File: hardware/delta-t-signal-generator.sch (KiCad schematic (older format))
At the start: 28 parts

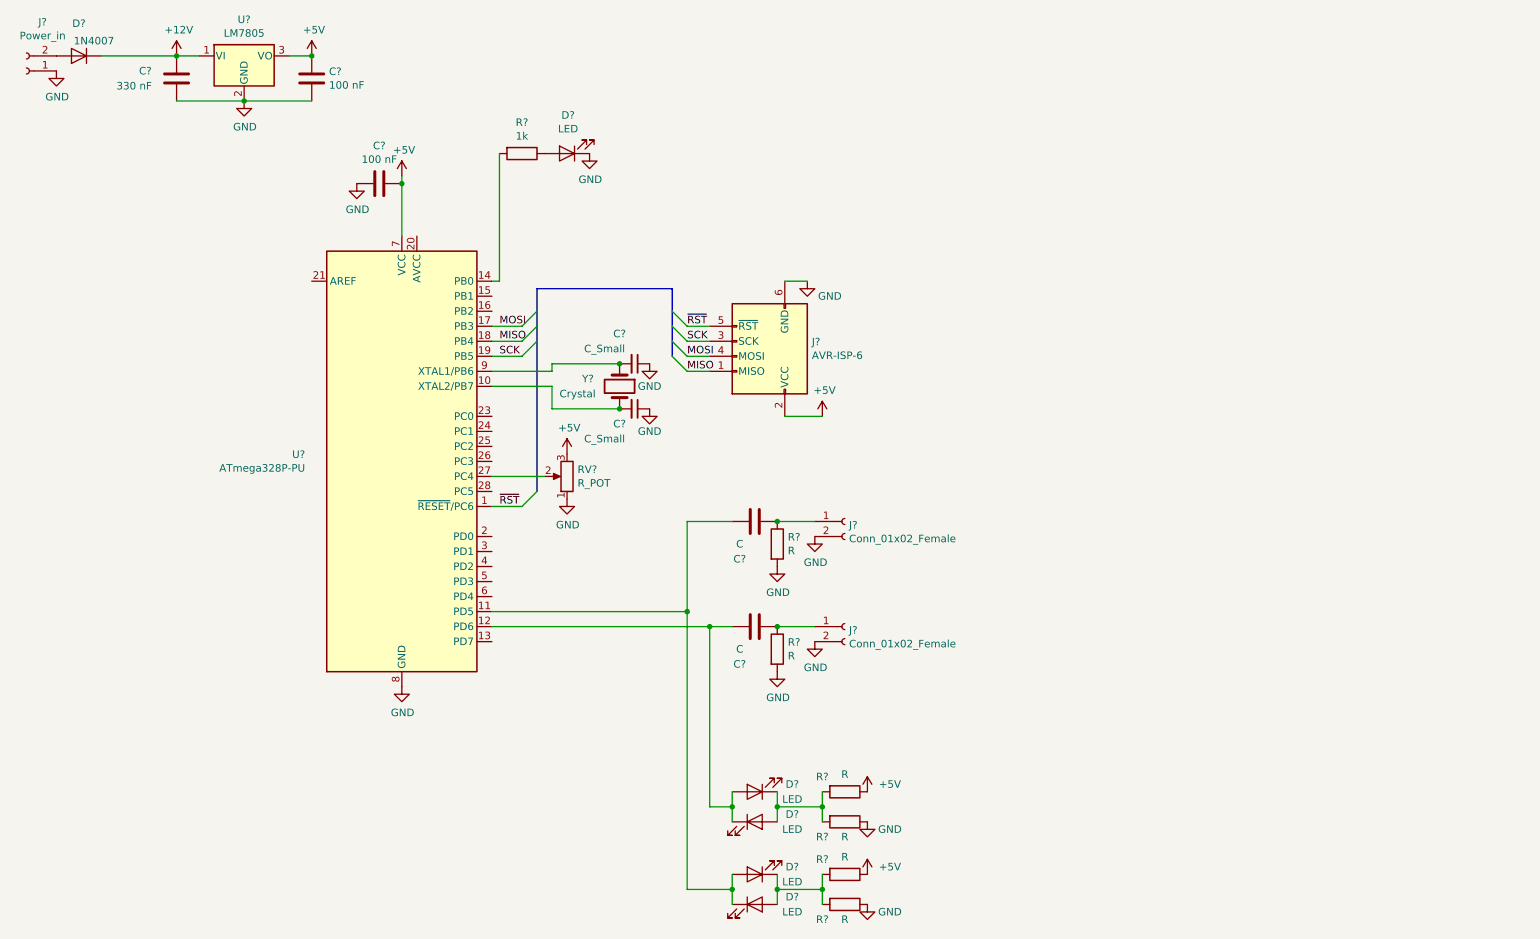
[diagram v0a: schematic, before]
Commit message: Update schematics to separate between board and cover parts
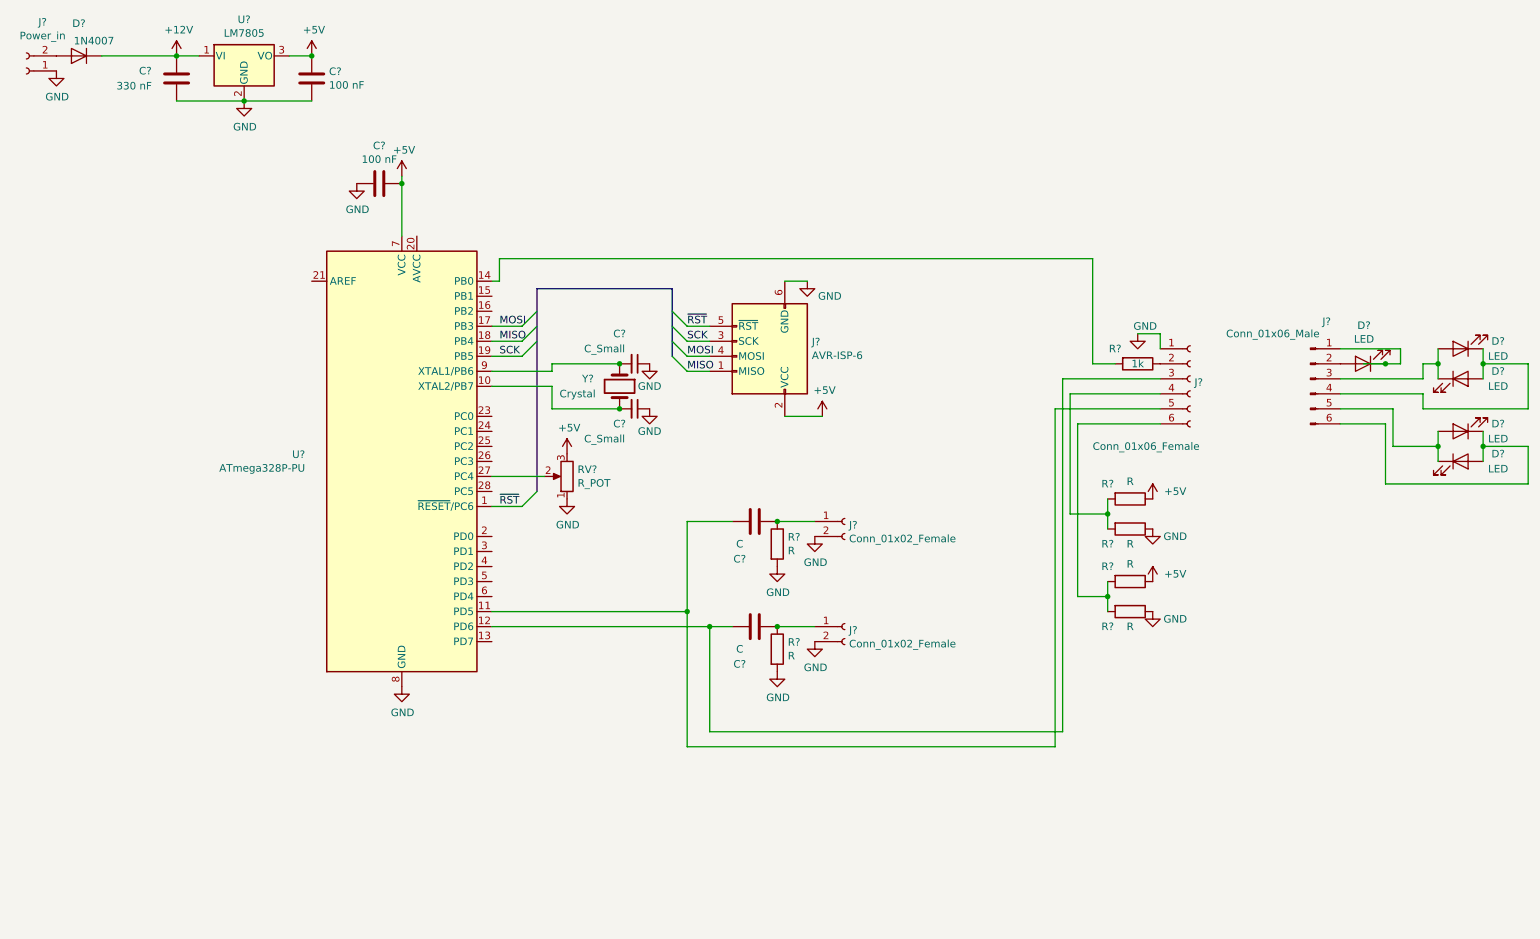
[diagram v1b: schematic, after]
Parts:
- added J?: Conn_01x06_Male, symbol Connector:Conn_01x06_Male
- added J?: Conn_01x06_Female, symbol Connector:Conn_01x06_Female
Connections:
- net GND: now also J?.1 (Pin_1); no longer D?.1 (K)
- net at R?.1: now also J?.2 (Pin_2); no longer D?.2 (A)
- net at C?.2, U?.11 (PD5): now also J?.5 (Pin_5); no longer D?.1 (K), D?.2 (A)
- net at C?.2, U?.12 (PD6): now also J?.3 (Pin_3); no longer D?.1 (K), D?.2 (A)
- net at D?.1 (K), D?.2 (A): now also J?.4 (Pin_4); no longer R?.2, R?.2
- net at D?.1 (K), D?.2 (A): now also J?.6 (Pin_6); no longer R?.2, R?.2
- new net: D?.1 (K), J?.1 (Pin_1)
- new net: D?.2 (A), J?.2 (Pin_2)
- new net: D?.1 (K), D?.2 (A), J?.3 (Pin_3)
- new net: D?.1 (K), D?.2 (A), J?.5 (Pin_5)
- new net: J?.4 (Pin_4), R?.2, R?.2
- new net: J?.6 (Pin_6), R?.2, R?.2
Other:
- moved on the sheet: D?, R?
